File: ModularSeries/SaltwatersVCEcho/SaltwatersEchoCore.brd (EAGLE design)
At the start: 74.8 x 100 mm, 110 parts, among them IC1 PT2399DIL16, Q1 2N3906, Q2 2N3906, Q3 2N3906, Q4 2N3906, Q5 2N3904, Q6 2N3904

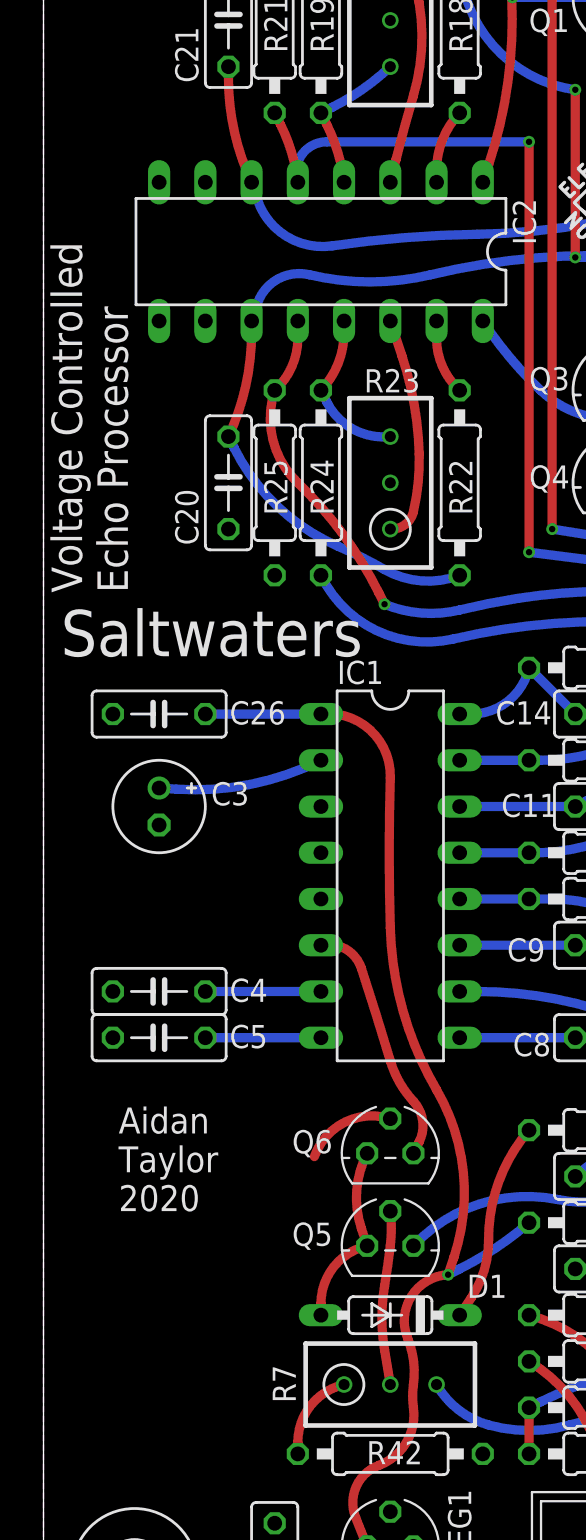
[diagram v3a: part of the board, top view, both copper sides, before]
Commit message: Saltwaters core further corrections to schematic
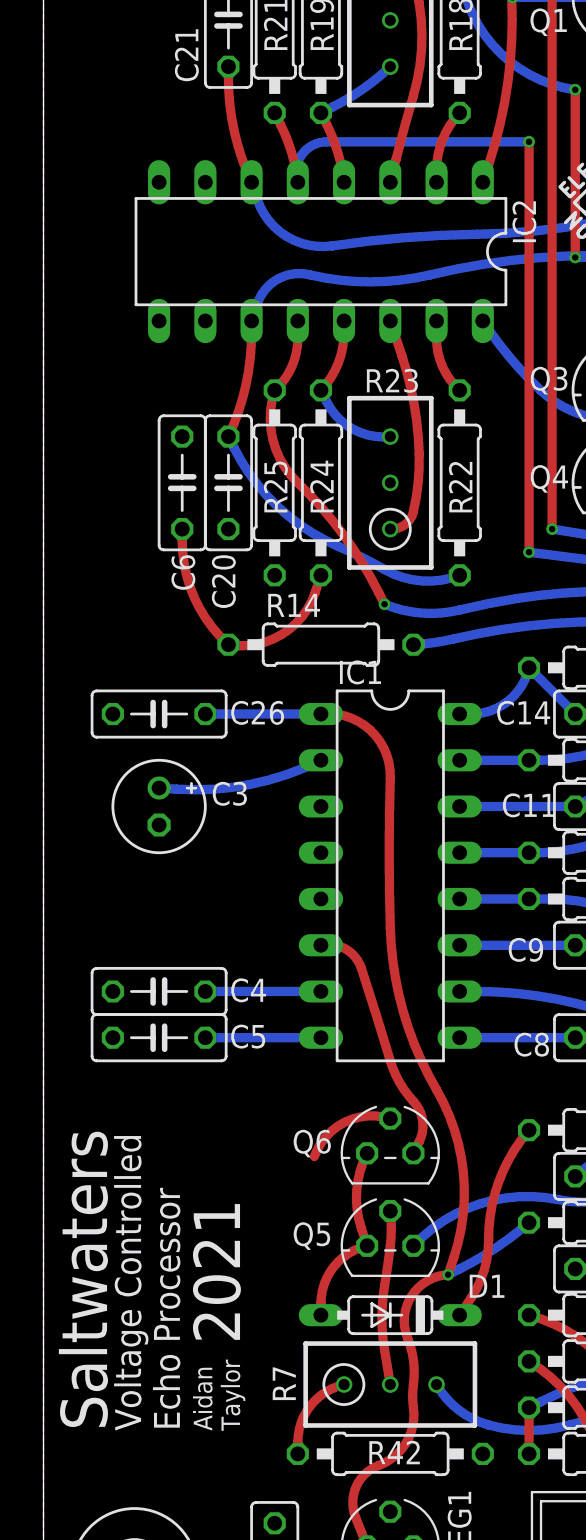
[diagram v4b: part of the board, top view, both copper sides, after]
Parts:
- added C6: 100nF, rcl:C050-025X075
- added R14: 1K, rcl:0207/10
- C10: value 10nF -> 4.7nF
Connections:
- new net N$8: C6.1, R14.1, R24.2
- net AGND: now also C6.2
- net DELAY_SIG: now also R14.2; no longer R24.2
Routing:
- net N$8: track 0.00 -> 13.4 mm
- net DELAY_SIG: track 60.1 -> 54.2 mm
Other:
- board text added: "2021"
- board text added: "Aidan Taylor"
- board text removed: "Aidan Taylor 2020"
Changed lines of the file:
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@@
 <text x="70.1675" y="16.51" size="1.016" layer="21" font="vector" ratio="12" rot="R90" align="center">3</text>
 <wire x1="69.215" y1="16.51" x2="69.215" y2="11.43" width="0.254" layer="21"/>
-<text x="4.1275" y="24.765" size="1.4224" layer="21" font="vector" ratio="16">Aidan
-Taylor
-2020</text>
-<text x="0.9525" y="56.515" size="2.54" layer="21" font="vector" ratio="16" rot="R180" align="center-right">Saltwaters</text>
-<text x="2.54" y="58.7375" size="1.6764" layer="21" font="vector" ratio="16" rot="R90" align="center-left">Voltage Controlled
+<text x="10.795" y="12.7" size="1.016" layer="21" font="vector" ratio="16" rot="R90">Aidan
+Taylor</text>
+<text x="2.2225" y="12.7" size="2.54" layer="21" font="vector" ratio="16" rot="R270" align="center-right">Saltwaters</text>
+<text x="5.715" y="12.7" size="1.4224" layer="21" font="vector" ratio="16" rot="R90" align="center-left">Voltage Controlled
 Echo Processor</text>
 <wire x1="0" y1="95" x2="0" y2="5" width="0" layer="20"/>
@@
 <wire x1="69.75" y1="100" x2="5" y2="100" width="0" layer="20"/>
 <wire x1="5" y1="100" x2="0" y2="95" width="0" layer="20" curve="90"/>
+<text x="10.795" y="17.4625" size="2.54" layer="21" font="vector" ratio="16" rot="R90">2021</text>
 </plain>
 <attributes>
@@
 <attribute name="VALUE" x="22.479" y="5.334" size="1.27" layer="27" ratio="10" rot="R180"/>
 </element>
-<element name="C10" library="rcl" library_urn="urn:adsk.eagle:library:334" package="C050-025X075" package3d_urn="urn:adsk.eagle:package:23637/1" value="10nF" x="44.45" y="43.18" smashed="yes" rot="R180">
+<element name="C10" library="rcl" library_urn="urn:adsk.eagle:library:334" package="C050-025X075" package3d_urn="urn:adsk.eagle:package:23637/1" value="4.7nF" x="44.45" y="43.18" smashed="yes" rot="R180">
 <attribute name="NAME" x="48.641" y="42.6085" size="1.27" layer="25" ratio="10"/>
 <attribute name="POPULARITY" value="29" x="27.94" y="78.74" size="1.778" layer="27" rot="R180" display="off"/>
@@
 </element>
 <element name="C20" library="rcl" library_urn="urn:adsk.eagle:library:334" package="C050-025X075" package3d_urn="urn:adsk.eagle:package:23637/1" value="100nF" x="10.16" y="64.77" smashed="yes" rot="R90">
-<attribute name="NAME" x="8.509" y="61.341" size="1.27" layer="25" ratio="10" rot="R90"/>
+<attribute name="NAME" x="9.271" y="60.8965" size="1.27" layer="25" ratio="10" rot="R270"/>
 <attribute name="POPULARITY" value="29" x="45.72" y="143.51" size="1.778" layer="27" rot="R90" display="off"/>
 <attribute name="SPICEPREFIX" value="C" x="45.72" y="143.51" size="1.778" layer="27" rot="R90" display="off"/>
@@
 <attribute name="SPICEPREFIXL" value="POT" x="44.45" y="49.53" size="1.778" layer="27" rot="R90" display="off"/>
 <attribute name="VALUE" x="48.95" y="53.48" size="1.27" layer="27" rot="R180"/>
+</element>
+<element name="R14" library="rcl" library_urn="urn:adsk.eagle:library:334" package="0207/10" package3d_urn="urn:adsk.eagle:package:23491/2" value="1K" x="15.24" y="55.88" smashed="yes">
+<attribute name="NAME" x="12.192" y="57.404" size="1.27" layer="25" ratio="10"/>
+<attribute name="POPULARITY" value="81" x="15.24" y="55.88" size="1.778" layer="27" display="off"/>
+<attribute name="SPICEPREFIX" value="R" x="15.24" y="55.88" size="1.778" layer="27" display="off"/>
+<attribute name="VALUE" x="12.9794" y="55.245" size="1.27" layer="27" ratio="10"/>
+</element>
+<element name="C6" library="rcl" library_urn="urn:adsk.eagle:library:334" package="C050-025X075" package3d_urn="urn:adsk.eagle:package:23637/1" value="100nF" x="7.62" y="64.77" smashed="yes" rot="R90">
+<attribute name="NAME" x="7.0485" y="60.8965" size="1.27" layer="25" ratio="10" rot="R270"/>
+<attribute name="POPULARITY" value="29" x="7.62" y="64.77" size="1.778" layer="27" rot="R90" display="off"/>
+<attribute name="SPICEPREFIX" value="C" x="7.62" y="64.77" size="1.778" layer="27" rot="R90" display="off"/>
+<attribute name="VALUE" x="10.414" y="61.341" size="1.27" layer="27" ratio="10" rot="R90"/>
 </element>
 </elements>
@@
 <contactref element="GND" pad="2"/>
 <contactref element="GND" pad="3"/>
+<contactref element="C6" pad="2"/>
 </signal>
 <signal name="N$1">
@@
 </signal>
 <signal name="DELAY_SIG">
-<contactref element="R24" pad="2"/>
 <contactref element="R39" pad="1"/>
 <contactref element="R36" pad="2"/>
@@
 <wire x1="31.75" y1="57.15" x2="30.7975" y2="57.15" width="0.508" layer="16"/>
 <wire x1="30.7975" y1="57.15" x2="22.5425" y2="56.1975" width="0.508" layer="16" curve="13.16389"/>
-<wire x1="22.5425" y1="56.1975" x2="15.24" y2="59.69" width="0.508" layer="16" curve="-77.447668"/>
 <wire x1="48.26" y1="29.21" x2="46.99" y2="29.5275" width="0.508" layer="16"/>
 <wire x1="46.99" y1="29.5275" x2="41.91" y2="33.02" width="0.508" layer="16" curve="-40.944555"/>
@@
 <wire x1="40.64" y1="35.8775" x2="37.465" y2="39.6875" width="0.508" layer="16" curve="53.79964"/>
 <wire x1="37.465" y1="39.6875" x2="31.75" y2="42.8625" width="0.508" layer="16" curve="-11.520017"/>
+<contactref element="R14" pad="2"/>
+<wire x1="22.5425" y1="56.1975" x2="20.32" y2="55.88" width="0.508" layer="16" curve="-10.067539"/>
 </signal>
 <signal name="N$24">
@@
 <wire x1="20.32" y1="63.1825" x2="19.05" y2="62.23" width="0.508" layer="1" curve="-80.255867"/>
 </signal>
+<signal name="N$8">
+<contactref element="R14" pad="1"/>
+<contactref element="C6" pad="1"/>
+<contactref element="R24" pad="2"/>
+<wire x1="15.24" y1="59.69" x2="14.9225" y2="58.7375" width="0.508" layer="1"/>
+<wire x1="14.9225" y1="58.7375" x2="10.16" y2="55.88" width="0.508" layer="1" curve="-81.202589"/>
+<wire x1="7.62" y1="62.23" x2="7.62" y2="61.595" width="0.508" layer="1"/>
+<wire x1="7.62" y1="61.595" x2="10.16" y2="55.88" width="0.508" layer="1" curve="47.924978"/>
+</signal>
 </signals>
